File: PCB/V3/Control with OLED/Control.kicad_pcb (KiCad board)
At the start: 2 copper layers, 41.9 x 48.3 mm, 9 parts, among them J1 L, J2 R, J3 OLED, J4 OLED, SW1 SW_Push, U1 ProMicro

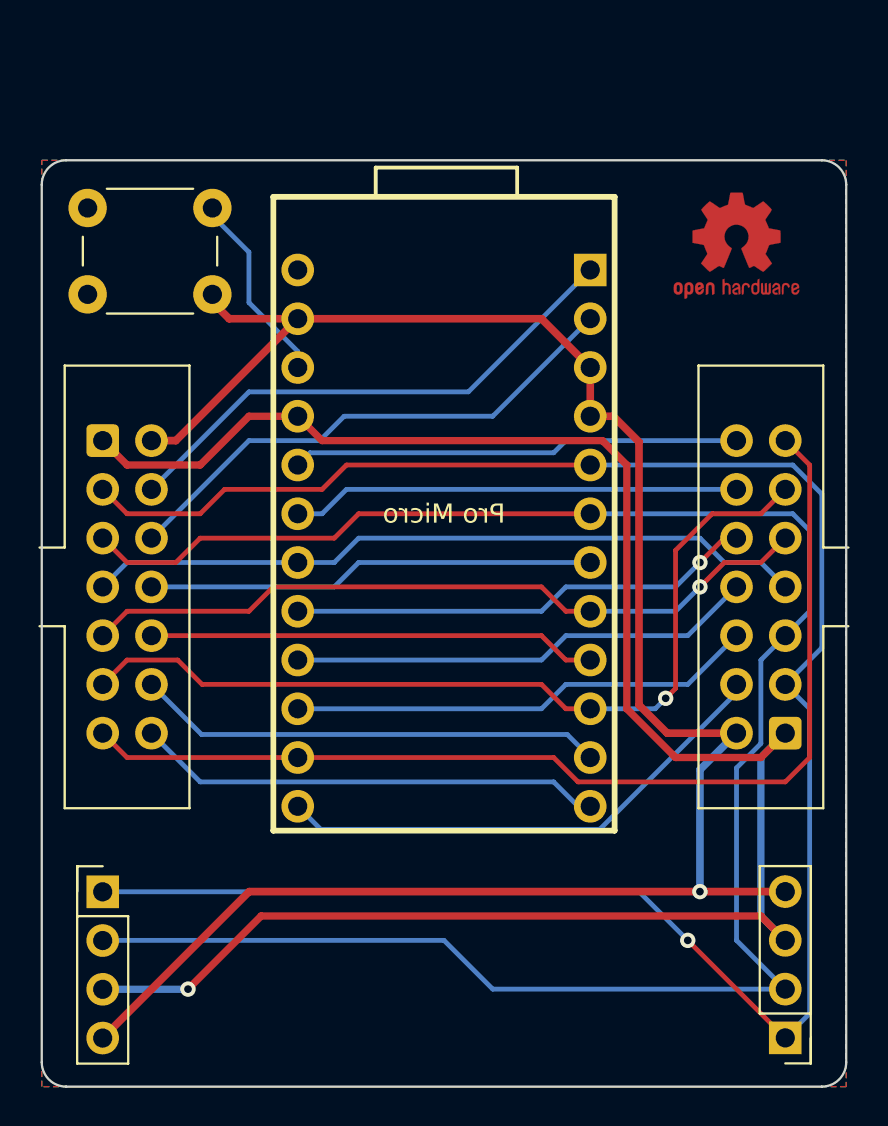
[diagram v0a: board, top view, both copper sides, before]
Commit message: fix silk screen
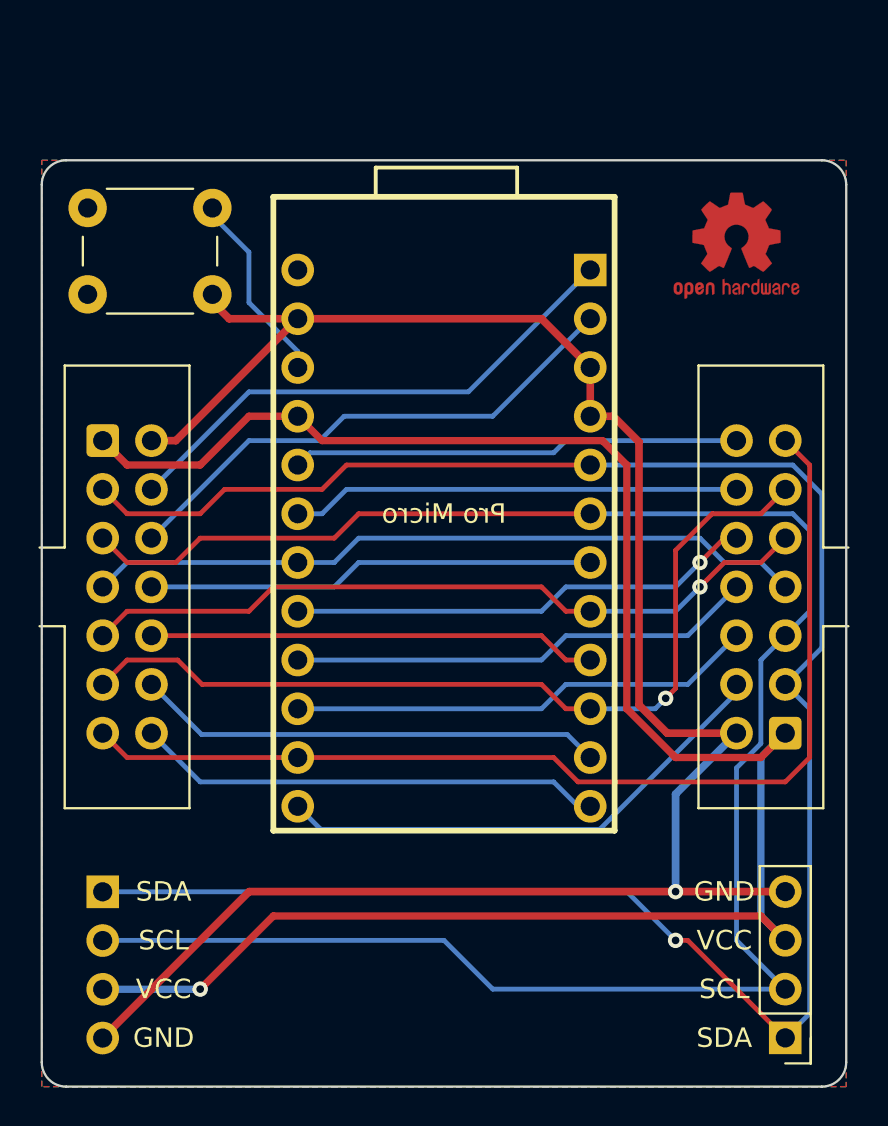
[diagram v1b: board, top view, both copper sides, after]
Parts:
- J3: moved to B.Cu
- turned J3 to 180 degrees
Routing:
- net GND: track 104.5 -> 105.0 mm

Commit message: update border.
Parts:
- added REF**: peek hole, Keyboard_JSA:peek hole, F.Cu at (144.1, 77.5)
- added REF**: peek hole, Keyboard_JSA:peek hole, F.Cu at (143.5, 57.1)
- added REF**: HRO-TYPE-C-31-M-12-Assembly, Keyboard_Keebio-Parts:HRO-TYPE-C-31-M-12-Assembly, F.Cu at (139.7, 44.5)
- added REF**: peek hole, Keyboard_JSA:peek hole, F.Cu at (135.3, 77.5)
- J3: moved to F.Cu
- U1: footprint Keyboard_JSA:ProMicro Reversed -> Keyboard_JSA:ProMicro Type C Reversed
- moved REF** 0.90 mm to (153.0, 54.0)
- turned J3 to 0 degrees
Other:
- outline, holes or cut-outs redrawn

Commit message: validating
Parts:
- removed the REF** at (144.1, 77.5)
- removed the REF** at (143.5, 57.1)
- removed the REF** at (139.7, 44.5)
- removed the REF** at (135.3, 77.5)
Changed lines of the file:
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@@
-    )
-  )
-  (footprint "Keyboard_JSA:peek hole" (layer "F.Cu")
-    (at 144.145 77.47)
-    (attr board_only exclude_from_bom)
-    (fp_text reference "REF**" (at 0 -2.54 unlocked) (layer "F.SilkS")
-      (effects (font (size 1 1) (thickness 0.15)))
-    )
-    (fp_text value "peek hole" (at 0 1 unlocked) (layer "F.Fab")
-      (effects (font (size 1 1) (thickness 0.15)))
-    )
-    (fp_text user "${REFERENCE}" (at 0 2.5 unlocked) (layer "F.Fab")
-      (effects (font (size 1 1) (thickness 0.15)))
-    )
-    (pad "" np_thru_hole circle (at 0 0) (size 1 1) (drill 1) (layers F&B.Cu *.Mask))
-  )
-  (footprint "Keyboard_JSA:peek hole" (layer "F.Cu")
-    (at 143.51 57.15)
-    (attr board_only exclude_from_bom)
-    (fp_text reference "REF**" (at 0 -2.54 unlocked) (layer "F.SilkS")
-      (effects (font (size 1 1) (thickness 0.15)))
-    )
-    (fp_text value "peek hole" (at 0 1 unlocked) (layer "F.Fab")
-      (effects (font (size 1 1) (thickness 0.15)))
-    )
-    (fp_text user "${REFERENCE}" (at 0 2.5 unlocked) (layer "F.Fab")
-      (effects (font (size 1 1) (thickness 0.15)))
-    )
-    (pad "" np_thru_hole circle (at 0 0) (size 1 1) (drill 1) (layers F&B.Cu *.Mask))
-  )
-  (footprint "Keyboard_Keebio-Parts:HRO-TYPE-C-31-M-12-Assembly" (layer "F.Cu")
-    (at 139.7 44.45 180)
-    (solder_mask_margin 0.05)
-    (solder_paste_margin 0.05)
-    (clearance 0.05)
-    (attr board_only exclude_from_pos_files exclude_from_bom)
-    (fp_text reference "REF**" (at 0 0.635) (layer "F.SilkS") hide
-      (effects (font (size 0.8 0.8) (thickness 0.15)))
-    )
-    (fp_text value "HRO-TYPE-C-31-M-12-Assembly" (at 0 1.15) (layer "Dwgs.User")
-      (effects (font (size 1 1) (thickness 0.15)))
-    )
-    (fp_text user "${REFERENCE}" (at 0 0) (layer "F.Fab")
-      (effects (font (size 1 1) (thickness 0.15)))
-    )
-    (fp_line (start 4.47 0) (end 4.47 -7.3) (layer "Dwgs.User") (width 0.15))
-    (fp_line (start -4.47 -7.3) (end 4.47 -7.3) (layer "Dwgs.User") (width 0.15))
-    (fp_line (start -4.47 0) (end -4.47 -7.3) (layer "Dwgs.User") (width 0.15))
-    (fp_line (start -4.47 0) (end 4.47 0) (layer "Dwgs.User") (width 0.15))
-    (fp_line (start 4.5 -7.5) (end 4.5 0) (layer "F.CrtYd") (width 0.15))
-    (fp_line (start -3.75 -7.5) (end -3.75 -8.5) (layer "F.CrtYd") (width 0.15))
-    (fp_line (start -3.75 -8.5) (end 3.75 -8.5) (layer "F.CrtYd") (width 0.15))
-    (fp_line (start -4.5 -7.5) (end -3.75 -7.5) (layer "F.CrtYd") (width 0.15))
-    (fp_line (start 4.5 -7.5) (end 3.75 -7.5) (layer "F.CrtYd") (width 0.15))
-    (fp_line (start -4.5 0) (end -4.5 -7.5) (layer "F.CrtYd") (width 0.15))
-    (fp_line (start 3.75 -8.5) (end 3.75 -7.5) (layer "F.CrtYd") (width 0.15))
-    (fp_line (start 4.5 0) (end -4.5 0) (layer "F.CrtYd") (width 0.15))
-    (pad "" np_thru_hole circle locked (at -2.89 -6.25 180) (size 0.65 0.65) (drill 0.65) (layers *.Cu *.Mask))
-    (pad "" np_thru_hole circle locked (at 2.89 -6.25 180) (size 0.65 0.65) (drill 0.65) (layers *.Cu *.Mask))
-    (pad "1" smd rect locked (at -3.225 -7.695 180) (size 0.6 1.45) (layers "F.Cu" "F.Paste" "F.Mask"))
-    (pad "2" smd rect locked (at -2.45 -7.695 180) (size 0.6 1.45) (layers "F.Cu" "F.Paste" "F.Mask"))
-    (pad "3" smd rect locked (at -1.75 -7.695 180) (size 0.3 1.45) (layers "F.Cu" "F.Paste" "F.Mask"))
-    (pad "4" smd rect locked (at -1.25 -7.695 180) (size 0.3 1.45) (layers "F.Cu" "F.Paste" "F.Mask"))
-    (pad "5" smd rect locked (at -0.75 -7.695 180) (size 0.3 1.45) (layers "F.Cu" "F.Paste" "F.Mask"))
-    (pad "6" smd rect locked (at -0.25 -7.695 180) (size 0.3 1.45) (layers "F.Cu" "F.Paste" "F.Mask"))
-    (pad "7" smd rect locked (at 0.25 -7.695 180) (size 0.3 1.45) (layers "F.Cu" "F.Paste" "F.Mask"))
-    (pad "8" smd rect locked (at 0.75 -7.695 180) (size 0.3 1.45) (layers "F.Cu" "F.Paste" "F.Mask"))
-    (pad "9" smd rect locked (at 1.25 -7.695 180) (size 0.3 1.45) (layers "F.Cu" "F.Paste" "F.Mask"))
-    (pad "10" smd rect locked (at 1.75 -7.695 180) (size 0.3 1.45) (layers "F.Cu" "F.Paste" "F.Mask"))
-    (pad "11" smd rect locked (at 2.45 -7.695 180) (size 0.6 1.45) (layers "F.Cu" "F.Paste" "F.Mask"))
-    (pad "12" smd rect locked (at 3.225 -7.695 180) (size 0.6 1.45) (layers "F.Cu" "F.Paste" "F.Mask"))
-    (pad "13" thru_hole oval locked (at -4.32 -2.6 180) (size 1 1.6) (drill oval 0.6 1.2) (layers *.Cu *.Mask))
-    (pad "13" thru_hole oval locked (at -4.32 -6.78 180) (size 1 2.1) (drill oval 0.6 1.7) (layers *.Cu *.Mask))
-    (pad "13" thru_hole oval locked (at 4.32 -6.78 180) (size 1 2.1) (drill oval 0.6 1.7) (layers *.Cu *.Mask))
-    (pad "13" thru_hole oval locked (at 4.32 -2.6 180) (size 1 1.6) (drill oval 0.6 1.2) (layers *.Cu *.Mask))
-    (model "/Users/james/Projects/Keyboard/KiCad_Lib/JSA/models/HRO-TYPE-C-31-M-12.step"
-      (offset (xyz -4.5 0 0))
-      (scale (xyz 1 1 1))
-      (rotate (xyz -90 0 0))
     )
   )
@@
     )
   )
-  (footprint "Keyboard_JSA:peek hole" (layer "F.Cu")
-    (at 135.255 77.47)
-    (attr board_only exclude_from_bom)
-    (fp_text reference "REF**" (at 0 -2.54 unlocked) (layer "F.SilkS")
-      (effects (font (size 1 1) (thickness 0.15)))
-    )
-    (fp_text value "peek hole" (at 0 1 unlocked) (layer "F.Fab")
-      (effects (font (size 1 1) (thickness 0.15)))
-    )
-    (fp_text user "${REFERENCE}" (at 0 2.5 unlocked) (layer "F.Fab")
-      (effects (font (size 1 1) (thickness 0.15)))
-    )
-    (pad "" np_thru_hole circle (at 0 0) (size 1 1) (drill 1) (layers F&B.Cu *.Mask))
-  )
   (footprint "Symbol:KiCad-Logo_5mm_Copper" (layer "B.Cu")
